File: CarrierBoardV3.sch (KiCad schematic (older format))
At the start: 86 parts, among them J1 USB_B_Micro, J11 Conn_02x26_Odd_Even, J2 Conn_02x09_Odd_Even, J3 Barrel_Jack, J4 TX2iConnctor, J5 Conn_02x04_Odd_Even, J6 Conn_01x03_Male, J7 Conn_02x03_Odd_Even, J8 Conn_02x26_Odd_Even, J9 Conn_01x03_Male, SW1 SW_Push, SW2 SW_Push, SW3 SW_Push, U1 MAX3221, U2 FT232RQ, U3 MSATA-Socket

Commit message: Part of Layout complete
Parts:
- removed C2: .1uF, Capacitor_SMD:C_0603_1608Metric, symbol Device:C
- removed C5: 4.7uF, Capacitor_SMD:C_0603_1608Metric, symbol Device:C
- J1: footprint Connectors_USB:USB_Micro-B_Molex-105017-0001 -> Connector_USB:USB_Micro-B_Molex-105017-0001
- L1, L2, L3: renamed from L?; footprint (none) -> Resistor_SMD:R_0603_1608Metric
- U6, U8: renamed from U?; footprint (none) -> CarrierBoardV3:QFN-20
- U7: renamed from U?; footprint (none) -> Package_SO:SOIC-8-1EP_3.9x4.9mm_P1.27mm_EP2.35x2.35mm
- gave numbers to parts that had none: 18
- renumbered C3 to C2, C12 to C21, C13 to C22, C14 to C26, C15 to C28, C4 to C3, C9 to C8, C8 to C9, J11 to J10, J6 to J5, J5 to J6, R17 to R19, R18 to R20, R19 to R21, R20 to R22, R21 to R23
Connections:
- net labels removed: SATA_ACTn, SPI0_POWER, SW1, SW2, TX2i_RX, TX2i_TX
- wire segments 325 -> 316
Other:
- note removed: "Cant find where to connect yet"
- note removed: "move 12v 3.3V 5v to switches\nrename 3v3 rtc and have it connected always on 3v3 rail."

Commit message: PCB Layout almost done, gnd fills and PC104 update needed
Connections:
- net labels removed: SPI0_CS#
- wire segments 316 -> 466

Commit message: Layout revisions
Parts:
- removed C10, C8: .33uF, Capacitor_SMD:CP_Elec_4x4.5, symbol Device:CP
- removed C21, C26: 10uF, Capacitor_SMD:CP_Elec_4x4.5, symbol Device:CP
- removed C22, C28: 22uF, Capacitor_SMD:CP_Elec_4x4.5, symbol Device:CP
- added C19, C24: 10uF, Capacitor_SMD:C_0603_1608Metric, symbol Device:C
- added C20, C26: 22uF, Capacitor_SMD:C_0603_1608Metric, symbol Device:C
- added C6, C8: .33uF, Capacitor_SMD:C_0603_1608Metric, symbol Device:C
- SW1, SW2, SW3: footprint Button_Switch_SMD:SW_SPST_B3S-1000 -> Button_Switch_SMD:SW_SPST_B3U-1000P
- renumbered C12 to C10, C13 to C11, C14 to C12, C15 to C13, C16 to C14, C17 to C15, C18 to C16, C19 to C17, C20 to C18, C23 to C21, C24 to C22, C25 to C23, C27 to C25, C29 to C27, C6 to C4, C7 to C5, C9 to C7, C11 to C9

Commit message: PCB touch up
Added shunts for SWs and fixed some trace shorts
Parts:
- added J11: SW1-12V_SHUNT, Jumper:SolderJumper-2_P1.3mm_Open_Pad1.0x1.5mm, symbol Connector:Conn_01x02_Male
- added J12: SW8-3V3_SHUNT, Jumper:SolderJumper-2_P1.3mm_Open_Pad1.0x1.5mm, symbol Connector:Conn_01x02_Male
- added J13: SW5-5V_SHUNT, Jumper:SolderJumper-2_P1.3mm_Open_Pad1.0x1.5mm, symbol Connector:Conn_01x02_Male
- renumbered TP3 to 12V1, TP1 to 3V3, TP2 to 5V1, SW1 to PWR1, SW2 to RESET1, SW3 to WAKE1
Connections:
- net TX2i_GND is gone; now on net GNDREF: J4.H46 (GND)
- net SW5: now also J13.1 (Pin_1)
- net SW8: now also J12.1 (Pin_1)
- net TX2i_12V: now also J11.2 (Pin_2); no longer J10.8 (Pin_8)
- net TX2i_3V3: now also J12.2 (Pin_2); no longer J10.12 (Pin_12)
- net TX2i_5V: now also J13.2 (Pin_2); no longer J10.10 (Pin_10), J8.32 (Pin_32)
- new net SW1: J10.8 (Pin_8), J11.1 (Pin_1)
- new net SW2: J10.10 (Pin_10)
- new net SW4: J10.12 (Pin_12)
- new net USB_CHG5V: J8.32 (Pin_32)

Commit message: finished schematic update for OBC and Tranciever
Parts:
- added NT?: SDA_B, NetTie:NetTie-2_SMD_Pad0.5mm, symbol Device:Net-Tie_2
- added NT?: SCL_B, NetTie:NetTie-2_SMD_Pad0.5mm, symbol Device:Net-Tie_2
- added NT?: SPI_A, NetTie:NetTie-2_SMD_Pad0.5mm, symbol Device:Net-Tie_2
- added NT?: SPI_CLK, NetTie:NetTie-2_SMD_Pad0.5mm, symbol Device:Net-Tie_2
- added NT?: SPI_MISO, NetTie:NetTie-2_SMD_Pad0.5mm, symbol Device:Net-Tie_2
- added NT?: SPI_MOSI, NetTie:NetTie-2_SMD_Pad0.5mm, symbol Device:Net-Tie_2
- added NT?: UART_TXJETSON, NetTie:NetTie-2_SMD_Pad0.5mm, symbol Device:Net-Tie_2
- added NT?: UART_RXJETSON, NetTie:NetTie-2_SMD_Pad0.5mm, symbol Device:Net-Tie_2
- J12: value SW8-3V3_SHUNT -> SW9-3V3_SHUNT
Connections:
- net I2C_GP1_CK: now also NT?.1; no longer J8.43 (Pin_43)
- net I2C_GP1_DAT: now also NT?.1; no longer J8.41 (Pin_41)
- net SPI0_CLK: now also NT?.1
- net SPI0_CS0#: now also NT?.1
- net SPI0_MISO: now also NT?.1
- net SPI0_MOSI: now also NT?.2
- net SW5: no longer J13.1 (Pin_1)
- net SW6: now also J13.1 (Pin_1)
- net SW8: no longer J12.1 (Pin_1)
- net SW9: now also J12.1 (Pin_1)
- net UART0_RX: now also NT?.2
- net UART0_TX: now also NT?.1
- net 3V3_PLAT: now reaches J10.27 (Pin_27)
- net 3V3_PLAT: now also J10.28 (Pin_28)
- net DTMF1: now reaches J10.49 (Pin_49)
- net DTMF2: now reaches J10.50 (Pin_50)
- net DTMF3: now reaches J10.51 (Pin_51)
- net DTMF4: now reaches J10.52 (Pin_52)
- net GPIO_A: now reaches J8.1 (Pin_1)
- net SPI_CS_B: now reaches J8.10 (Pin_10)
- net SPI_CS_C: now reaches J8.11 (Pin_11)
- net SPI_CS_D: now reaches J8.12 (Pin_12)
- net SPI_CS_E: now reaches J8.13 (Pin_13)
- net SPI_CS_F: now reaches J8.14 (Pin_14)
- net GPIO_J: now reaches J8.15 (Pin_15)
- net GPIO_K: now reaches J8.16 (Pin_16)
- net GPIO_L: now reaches J8.17 (Pin_17)
- net GPIO_M: now reaches J8.18 (Pin_18)
- net GPIO_B: now reaches J8.2 (Pin_2)
- net SPI_CLK: now reaches J8.21 (Pin_21)
- net SPI_CLK: now also NT?.2
- net SPI_MISO: now reaches J8.22 (Pin_22)
- net SPI_MISO: now also NT?.2
- net SPI_MOSI: now reaches J8.23 (Pin_23)
- net SPI_MOSI: now also NT?.1
- net SPI_CS: now reaches J8.24 (Pin_24)
- net GPIO_R: now reaches J8.27 (Pin_27)
- net GPIO_S: now reaches J8.28 (Pin_28)
- net GPIO_T: now reaches J8.29 (Pin_29)
- net GPIO_C: now reaches J8.3 (Pin_3)
- net GPIO_U: now reaches J8.30 (Pin_30)
- net GPIO_V: now reaches J8.31 (Pin_31)
- net UART_B_RX_LVTTL_GPS: now reaches J8.34 (Pin_34)
- net UART_B_TX_LVTTL_GPS: now reaches J8.36 (Pin_36)
- net UART_C_RS485+: now reaches J8.37 (Pin_37)
- net UART_E_RS485+: now reaches J8.38 (Pin_38)
- net UART_C_RS485-: now reaches J8.39 (Pin_39)
- net GPIO_D: now reaches J8.4 (Pin_4)
- net UART_E_RS485-: now reaches J8.40 (Pin_40)
- net CAN_H: now reaches J8.42 (Pin_42)
- net CAN_L: now reaches J8.44 (Pin_44)
- net SDA_B: now reaches J8.45 (Pin_45)
- net SDA_B: now also NT?.2
- net SCL_B: now reaches J8.47 (Pin_47)
- net SCL_B: now also NT?.2
- net GPIO_E: now reaches J8.5 (Pin_5)
- net GPIO_F: now reaches J8.6 (Pin_6)
- net GPIO_G: now reaches J8.7 (Pin_7)
- net GPIO_H: now reaches J8.8 (Pin_8)
- net SPI_CS_A: now reaches J8.9 (Pin_9)
- net SPI_CS_A: now also NT?.2
- net TX2i_VBATT renamed VBATT
- new net SCL_A: J8.43 (Pin_43)
- new net SDA_A: J8.41 (Pin_41)
- new net UART_A_RX_LVTTL: NT?.2
- new net UART_A_TX_LVTTL: NT?.1
- no-connect marks 64 -> 59
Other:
- note added: "UART"
- note removed: "Rs232"

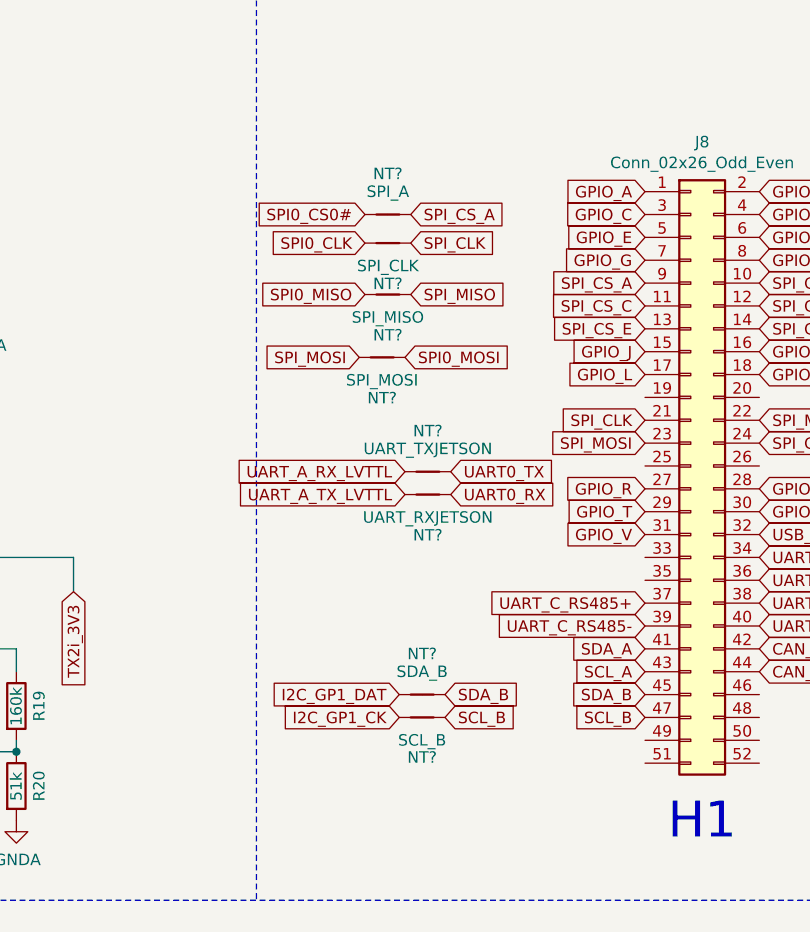
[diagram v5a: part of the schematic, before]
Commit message: Routed all new edits done to PC104
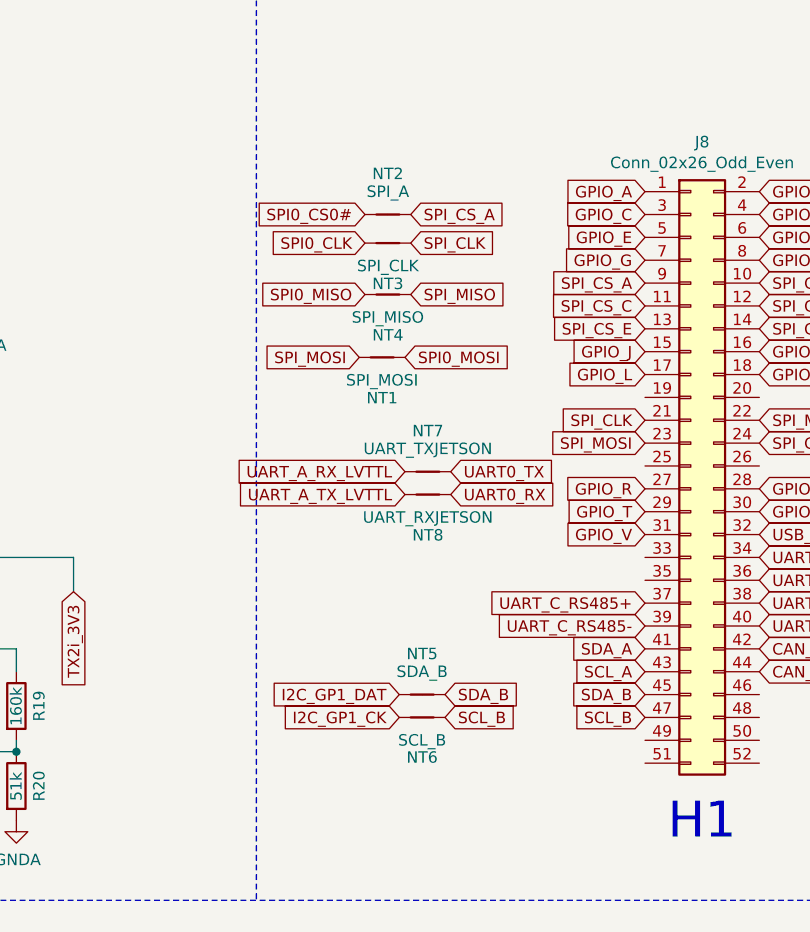
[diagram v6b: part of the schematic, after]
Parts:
- gave numbers to parts that had none: 8
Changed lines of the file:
@@
 SCL_B
 $Comp
-L Device:Net-Tie_2 NT?
+L Device:Net-Tie_2 NT5
 U 1 1 5CADBADF
 P 17875 7350
-F 0 "NT?" H 17875 7528 50  0000 C CNN
+F 0 "NT5" H 17875 7528 50  0000 C CNN
 F 1 "SDA_B" H 17875 7450 50  0000 C CNN
 F 2 "NetTie:NetTie-2_SMD_Pad0.5mm" H 17875 7350 50  0001 C CNN
@@
 $EndComp
 $Comp
-L Device:Net-Tie_2 NT?
+L Device:Net-Tie_2 NT6
 U 1 1 5CBE0A0C
 P 17875 7450
-F 0 "NT?" H 17875 7275 50  0000 C CNN
+F 0 "NT6" H 17875 7275 50  0000 C CNN
 F 1 "SCL_B" H 17875 7350 50  0000 C CNN
 F 2 "NetTie:NetTie-2_SMD_Pad0.5mm" H 17875 7450 50  0001 C CNN
@@
 SPI_CS_A
 $Comp
-L Device:Net-Tie_2 NT?
+L Device:Net-Tie_2 NT2
 U 1 1 5CE928E0
 P 17725 5250
-F 0 "NT?" H 17725 5428 50  0000 C CNN
+F 0 "NT2" H 17725 5428 50  0000 C CNN
 F 1 "SPI_A" H 17725 5350 50  0000 C CNN
 F 2 "NetTie:NetTie-2_SMD_Pad0.5mm" H 17725 5250 50  0001 C CNN
@@
 SPI_CLK
 $Comp
-L Device:Net-Tie_2 NT?
+L Device:Net-Tie_2 NT3
 U 1 1 5D09B242
 P 17725 5375
-F 0 "NT?" H 17725 5553 50  0000 C CNN
+F 0 "NT3" H 17725 5553 50  0000 C CNN
 F 1 "SPI_CLK" H 17725 5475 50  0000 C CNN
 F 2 "NetTie:NetTie-2_SMD_Pad0.5mm" H 17725 5375 50  0001 C CNN
@@
 SPI_MISO
 $Comp
-L Device:Net-Tie_2 NT?
+L Device:Net-Tie_2 NT4
 U 1 1 5D26FD24
 P 17725 5600
-F 0 "NT?" H 17725 5778 50  0000 C CNN
+F 0 "NT4" H 17725 5778 50  0000 C CNN
 F 1 "SPI_MISO" H 17725 5700 50  0000 C CNN
 F 2 "NetTie:NetTie-2_SMD_Pad0.5mm" H 17725 5600 50  0001 C CNN
@@
 SPI_MOSI
 $Comp
-L Device:Net-Tie_2 NT?
+L Device:Net-Tie_2 NT1
 U 1 1 5D3DC548
 P 17700 5875
-F 0 "NT?" H 17700 6053 50  0000 C CNN
+F 0 "NT1" H 17700 6053 50  0000 C CNN
 F 1 "SPI_MOSI" H 17700 5975 50  0000 C CNN
 F 2 "NetTie:NetTie-2_SMD_Pad0.5mm" H 17700 5875 50  0001 C CNN
@@
 UART0_RX
 $Comp
-L Device:Net-Tie_2 NT?
+L Device:Net-Tie_2 NT7
 U 1 1 5D6ECBB9
 P 17900 6375
-F 0 "NT?" H 17900 6553 50  0000 C CNN
+F 0 "NT7" H 17900 6553 50  0000 C CNN
 F 1 "UART_TXJETSON" H 17900 6475 50  0000 C CNN
 F 2 "NetTie:NetTie-2_SMD_Pad0.5mm" H 17900 6375 50  0001 C CNN
@@
 $EndComp
 $Comp
-L Device:Net-Tie_2 NT?
+L Device:Net-Tie_2 NT8
 U 1 1 5D8253A8
 P 17900 6475
-F 0 "NT?" H 17900 6653 50  0000 C CNN
+F 0 "NT8" H 17900 6653 50  0000 C CNN
 F 1 "UART_RXJETSON" H 17900 6575 50  0000 C CNN
 F 2 "NetTie:NetTie-2_SMD_Pad0.5mm" H 17900 6475 50  0001 C CNN

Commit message: Finished Ready for FAB
S/N:0C137_V3_SP19
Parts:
- J13: value SW5-5V_SHUNT -> SW6-5V_SHUNT
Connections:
- net UART_A_RX_LVTTL: now also J8.33 (Pin_33)
- net UART_A_TX_LVTTL: now also J8.35 (Pin_35)
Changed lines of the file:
@@
 P 22250 7800
 F 0 "J13" V 22310 7840 50  0000 L CNN
-F 1 "SW5-5V_SHUNT" V 22401 7840 50  0000 L CNN
+F 1 "SW6-5V_SHUNT" V 22401 7840 50  0000 L CNN
 F 2 "Jumper:SolderJumper-2_P1.3mm_Open_Pad1.0x1.5mm" H 22250 7800 50  0001 C CNN
 F 3 "~" H 22250 7800 50  0001 C CNN
@@
 	1    0    0    1
 $EndComp
+Text GLabel 18850 6750 0    50   Input ~ 0
+UART_A_RX_LVTTL
+Text GLabel 18850 6850 0    50   Input ~ 0
+UART_A_TX_LVTTL
 $EndSCHEMATC

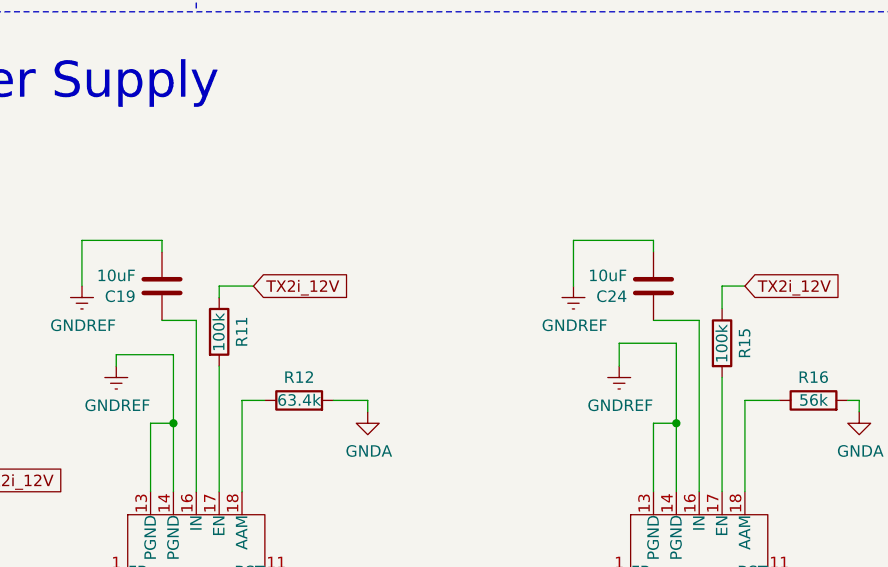
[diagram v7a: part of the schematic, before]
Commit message: Voltage regulator trace fix
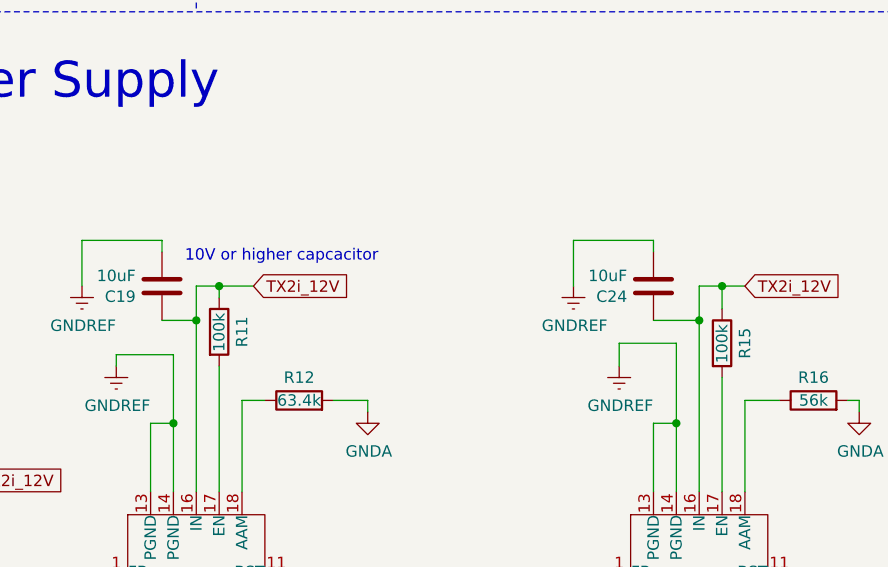
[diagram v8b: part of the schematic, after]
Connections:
- net TX2i_12V: now also C19.1, C24.1, U6.16 (IN), U8.16 (IN)
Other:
- note added: "10V or higher capcacitor\n"
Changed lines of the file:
@@
 	13050 6000 13050 5250
 Wire Wire Line
-	13050 5250 12900 5250
-Wire Wire Line
 	12950 6000 12950 5700
 Wire Wire Line
@@
 Text GLabel 18850 6850 0    50   Input ~ 0
 UART_A_TX_LVTTL
+Wire Wire Line
+	13050 5250 13050 5100
+Connection ~ 13150 5100
+Wire Wire Line
+	15250 5250 15250 5100
+Wire Wire Line
+	15250 5100 15350 5100
+Connection ~ 15250 5250
+Connection ~ 15350 5100
+Text Notes 13000 5000 0    50   ~ 0
+10V or higher capcacitor\n
+Wire Wire Line
+	13050 5100 13150 5100
+Connection ~ 13050 5250
+Wire Wire Line
+	12900 5250 13050 5250
 $EndSCHEMATC
